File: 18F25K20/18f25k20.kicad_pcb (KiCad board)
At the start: 2 copper layers, 33 parts, among them P1 CONN_01X02, P2 ICSP, U1 18F25K20, U2 LM1117

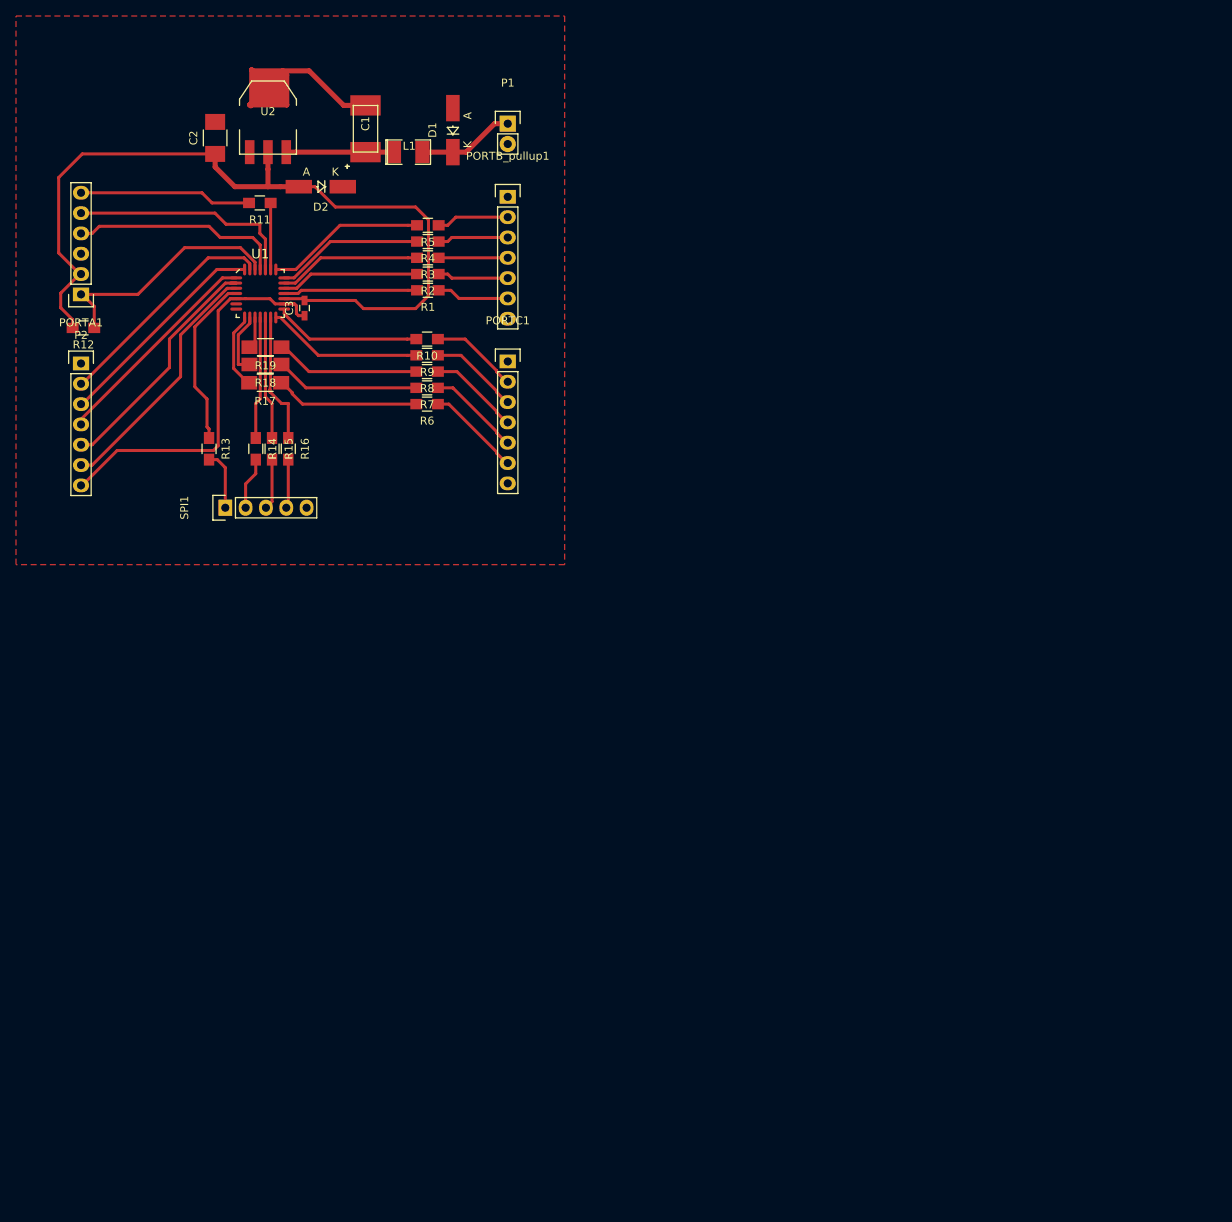
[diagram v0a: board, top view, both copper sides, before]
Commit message: PIC-ssop, sch &layout. TODO:modify pinheader+gnd polygon. 3.2mm holes
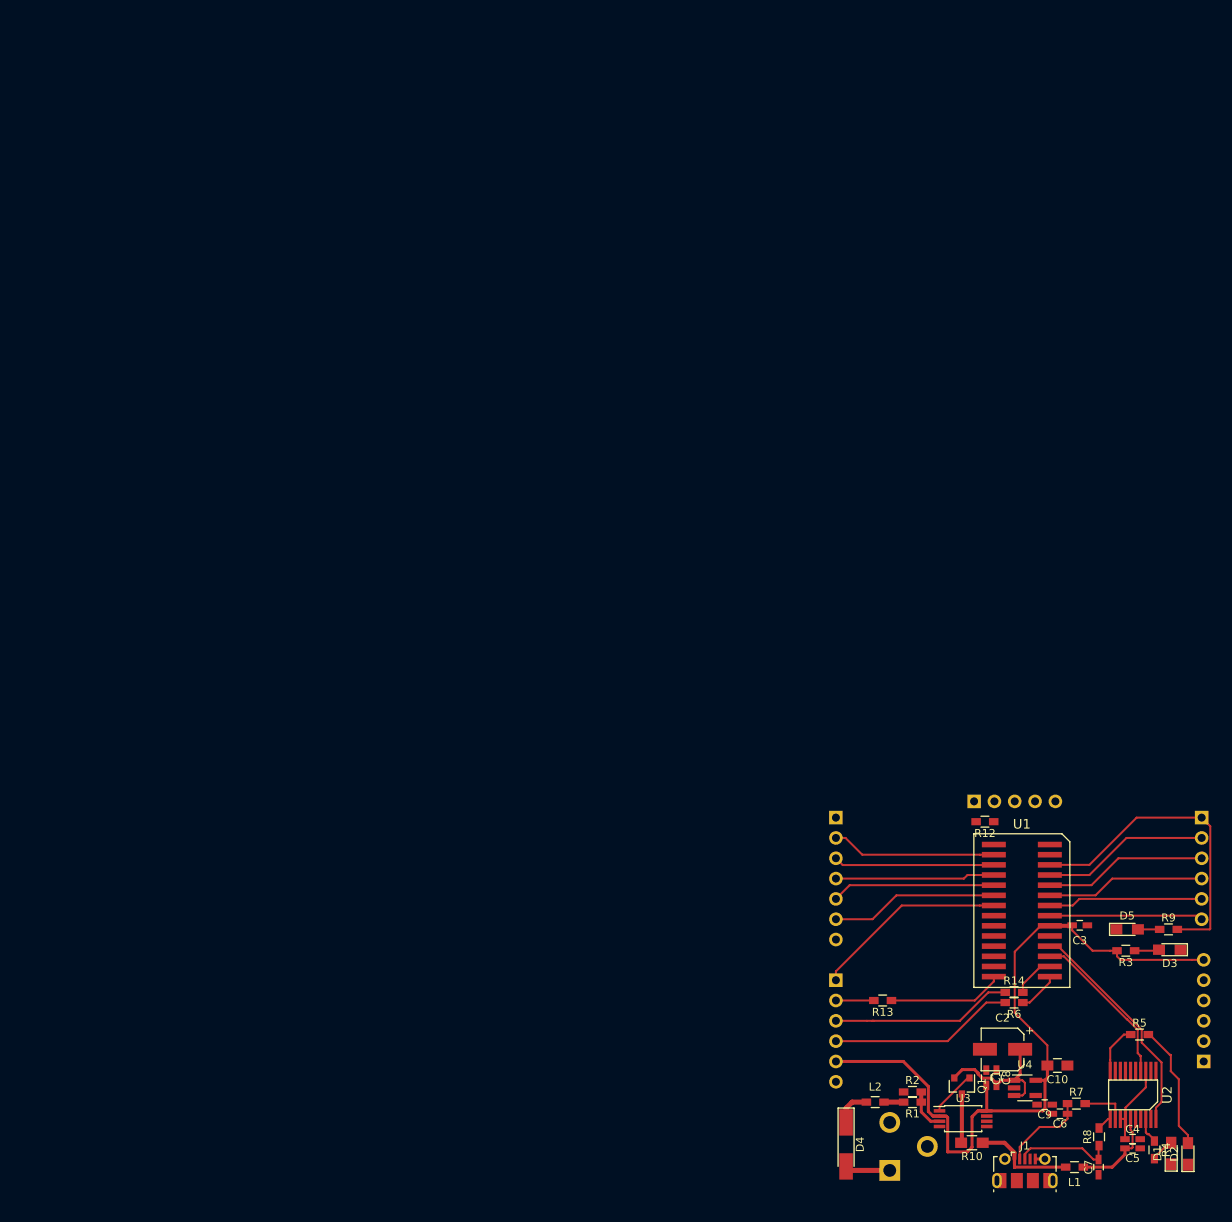
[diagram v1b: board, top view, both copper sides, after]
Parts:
- removed PORTA1, PORTB_pullup1, PORTC1: CONN_01X07, Pin_Headers:Pin_Header_Straight_1x07
- removed R11: 0, Resistors_SMD:R_0805_HandSoldering
- removed R15, R16: 220R, Resistors_SMD:R_0805_HandSoldering
- removed R17, R18, R19: 0, Resistors_SMD:R_1206_HandSoldering
- removed SPI1: CONN_01X05, Pin_Headers:Pin_Header_Straight_1x05
- added C10: 4u7, Capacitors_SMD:C_0805_HandSoldering, F.Cu at (219.5, 147.8)
- added C4: 100n, Capacitors_SMD:C_0603_HandSoldering, F.Cu at (228.9, 157.0)
- added C5: 100n, Capacitors_SMD:C_0603_HandSoldering, F.Cu at (228.9, 158.2)
- added C6: 47p, Capacitors_SMD:C_0603_HandSoldering, F.Cu at (219.8, 153.9)
- added C7: 47p, Capacitors_SMD:C_0603_HandSoldering, F.Cu at (224.6, 160.5)
- added C8: 1u, Capacitors_SMD:C_0603_HandSoldering, F.Cu at (211.8, 149.3)
- added C9: 10n, Capacitors_SMD:C_0603_HandSoldering, F.Cu at (217.9, 152.7)
- added D3: LED, LEDs:LED_0805_HandSoldering, F.Cu at (233.5, 133.3)
- added D4: LL4148, Diodes_SMD:D_MiniMELF_Handsoldering, F.Cu at (193.0, 157.7)
- added D5: LED, LEDs:LED_0805_HandSoldering, F.Cu at (228.2, 130.8)
- added J1: USB_OTG, Connectors_USB:USB_Micro-B_Molex-105017-0001, F.Cu at (215.4, 161.9)
- added J2: Barrel_Jack, Connectors:Barrel_Jack_CUI_PJ-102AH, B.Cu at (198.5, 160.9)
- added L2: FB, Inductors_SMD:L_0603_HandSoldering, F.Cu at (196.7, 152.4)
- added P3: PORTB, Pin_Headers:Pin_Header_Straight_1x06_Pitch2.54mm, B.Cu at (237.5, 116.8)
- added P4: PC_power, Pin_Headers:Pin_Header_Straight_1x06_Pitch2.54mm, B.Cu at (237.7, 147.3)
- added P5: ADC, Pin_Headers:Pin_Header_Straight_1x07_Pitch2.54mm, B.Cu at (191.8, 116.8)
- added Q1: FDN240P, TO_SOT_Packages_SMD:SOT-23, F.Cu at (207.5, 150.4)
- added U3: LM358, Housings_SSOP:TSSOP-8_4.4x3mm_Pitch0.65mm, F.Cu at (207.7, 154.5)
- added U4: LP2985-3.3, TO_SOT_Packages_SMD:SOT-23-5_HandSoldering, F.Cu at (215.4, 150.6)
- C1: value 100u -> 100n; footprint .pretty:2312_handsoldering -> Capacitors_SMD:C_0603_HandSoldering
- C2: value 33u -> 10u; footprint Capacitors_SMD:C_1210_HandSoldering -> Capacitors_SMD:CP_Elec_5x5.3
- D1: value 5V6 -> LED; footprint Diodes_SMD:MiniMELF_Handsoldering -> LEDs:LED_0805_HandSoldering
- D2: value LL914 -> LED; footprint Diodes_SMD:MiniMELF_Handsoldering -> LEDs:LED_0805_HandSoldering
- L1: value 4u7 -> FB; footprint SMD_Packages:SMD-1210_Pol -> Inductors_SMD:L_0603_HandSoldering
- P1: value CONN_01X02 -> SPI; footprint Pin_Headers:Pin_Header_Straight_1x02 -> Pin_Headers:Pin_Header_Straight_1x06_Pitch2.54mm; moved to B.Cu
- P2: footprint Pin_Headers:Pin_Header_Straight_1x06 -> Pin_Headers:Pin_Header_Straight_1x05_Pitch2.54mm; moved to B.Cu
- R1, R2: value 220R -> 10k; footprint Resistors_SMD:R_0805_HandSoldering -> Resistors_SMD:R_0603_HandSoldering
- R10: value 220R -> 0R
- R12, R13, R14, R6: footprint Resistors_SMD:R_0805_HandSoldering -> Resistors_SMD:R_0603_HandSoldering
- R3, R4, R5, R9: value 220R -> 270R; footprint Resistors_SMD:R_0805_HandSoldering -> Resistors_SMD:R_0603_HandSoldering
- R7, R8: value 220R -> 27R; footprint Resistors_SMD:R_0805_HandSoldering -> Resistors_SMD:R_0603_HandSoldering
- U1: value 18F25K20 -> 18F25K20_ssop; footprint .pretty:QFP_28 -> .pretty:SSOP-28_hand_solder
- U2: value LM1117 -> FTDI231x; footprint .pretty:SOT-223_handsoldering -> .pretty:SSOP-20_FTD23x
- moved D2 162.4 mm to (235.8, 158.9), turned to 90 degrees
- moved U2 156.8 mm to (225.2, 146.2), turned to 270 degrees
- moved D1 156.3 mm to (233.7, 158.8)
- moved L1 151.8 mm to (221.6, 160.5), turned to 180 degrees
- moved C2 150.5 mm to (212.6, 145.8), turned to 180 degrees
- moved R4 145.4 mm to (231.6, 158.4), turned to 270 degrees
- moved C1 141.9 mm to (210.6, 149.4), turned to 270 degrees
- moved R5 134.7 mm to (229.7, 144.0), turned to 0 degrees
- moved R12 128.5 mm to (210.4, 117.3)
- moved P2 128.4 mm to (209.0, 114.8), turned to 270 degrees
- moved R8 127.3 mm to (224.7, 156.7), turned to 90 degrees
- moved C3 123.9 mm to (222.2, 130.3), turned to 180 degrees
- moved R3 122.9 mm to (228.0, 133.5)
- moved U1 122.5 mm to (215.0, 128.5), turned to 270 degrees
- moved R10 121.4 mm to (208.8, 157.5)
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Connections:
- C1 pad 1: Net-(C1-Pad1) -> GND
- C1 pad 2: GND -> VCC
- C2 pad 1: Net-(C2-Pad1) -> /Vin
- C3 pad 2: Net-(C2-Pad1) -> VCC
- D1 pad 1: Net-(D1-Pad1) -> GND
- D1 pad 2: GND -> Net-(D1-Pad2)
- D2 pad 1: Net-(D2-Pad1) -> GND
- D2 pad 2: Net-(C2-Pad1) -> Net-(D2-Pad2)
- L1 pad 1: Net-(C1-Pad1) -> Net-(C5-Pad2)
- L1 pad 2: Net-(D1-Pad1) -> Net-(J1-Pad1)
- P1 pad 1: Net-(D1-Pad1) -> /SS
- P1 pad 2: GND -> /SCK
- P2 pad 2: Net-(C2-Pad1) -> VCC
- R1 pad 1: Net-(PORTB_pullup1-Pad6) -> /Vin_cmp
- R1 pad 2: Net-(R1-Pad2) -> /ps
- R10 pad 1: Net-(PORTC1-Pad2) -> /Vusb
- R10 pad 2: Net-(R10-Pad2) -> Net-(C5-Pad2)
- R12 pad 2: Net-(C2-Pad1) -> VCC
- R13 pad 1: Net-(R13-Pad1) -> /SCK
- R13 pad 2: Net-(R13-Pad2) -> /SCK
- R14 pad 1: Net-(R14-Pad1) -> /SDO
- R14 pad 2: Net-(R14-Pad2) -> /SDO
- R2 pad 1: Net-(PORTB_pullup1-Pad5) -> GND
- R2 pad 2: Net-(R2-Pad2) -> /Vin_cmp
- R3 pad 2: Net-(R3-Pad2) -> VCC
- R4 pad 1: Net-(PORTB_pullup1-Pad3) -> /Rx_led
- R4 pad 2: Net-(R4-Pad2) -> Net-(D1-Pad2)
- R5 pad 1: Net-(PORTB_pullup1-Pad2) -> /Tx_led
- R5 pad 2: Net-(R5-Pad2) -> Net-(D2-Pad2)
- R6 pad 1: Net-(PORTC1-Pad6) -> /SDI
- R6 pad 2: Net-(R17-Pad1) -> /SDI
- R7 pad 2: Net-(R18-Pad1) -> /D-
- R8 pad 2: Net-(R19-Pad1) -> /D+
- R9 pad 2: Net-(R9-Pad2) -> /picled
- U1 pad 1: Net-(PORTA1-Pad4) -> Net-(P2-Pad1)
- U1 pad 10: Net-(R19-Pad2) -> (no net)
- U1 pad 11: Net-(R14-Pad1) -> Net-(P4-Pad3)
- U1 pad 14: Net-(R9-Pad2) -> /SCK
- U1 pad 15: Net-(R10-Pad2) -> /SDI
- U1 pad 16: GND -> /SDO
- U1 pad 17: Net-(C2-Pad1) -> /RXD
- U1 pad 18: Net-(R1-Pad2) -> /TXD
- U1 pad 19: Net-(R2-Pad2) -> GND
- U1 pad 20: Net-(R3-Pad2) -> VCC
- U1 pad 21: Net-(R4-Pad2) -> Net-(P3-Pad6)
- U1 pad 22: Net-(R5-Pad2) -> Net-(P3-Pad5)
- U1 pad 24: Net-(P2-Pad5) -> Net-(P3-Pad3)
- U1 pad 25: Net-(P2-Pad4) -> Net-(P3-Pad2)
- U1 pad 26: Net-(P2-Pad1) -> /picled
- U1 pad 27: Net-(PORTA1-Pad2) -> Net-(P2-Pad5)
- U1 pad 28: Net-(PORTA1-Pad3) -> Net-(P2-Pad4)
- U1 pad 4: Net-(R13-Pad1) -> Net-(P5-Pad4)
- U1 pad 5: GND -> Net-(P5-Pad5)
- U1 pad 7: Net-(U1-Pad7) -> /SS
- U1 pad 8: Net-(R17-Pad2) -> GND
- U1 pad 9: Net-(R18-Pad2) -> (no net)
- U2 pad 1: GND -> (no net)
- U2 pad 2: Net-(C2-Pad1) -> (no net)
- U2 pad 3: Net-(C1-Pad1) -> Net-(C4-Pad1)
- U2 pad 4: (no net) -> /RXD
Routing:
- net Net-(C2-Pad1): track 106.6 -> 0.00 mm
- net VCC: track 0.00 -> 93.6 mm
- net GND: track 88.3 -> 1.20 mm
- net /picled: track 0.00 -> 39.9 mm
- net Net-(P2-Pad1): track 30.8 -> 0.00 mm
- net /TXD: track 0.00 -> 29.4 mm
- net Net-(P2-Pad5): track 28.9 -> 0.00 mm
- net Net-(PORTA1-Pad2): track 28.7 -> 0.00 mm
- net /SDI: track 0.00 -> 28.3 mm
- net /SDO: track 0.00 -> 28.1 mm
- net Net-(PORTA1-Pad4): track 27.5 -> 0.00 mm
- net Net-(PORTA1-Pad3): track 27.4 -> 0.00 mm
- net Net-(P2-Pad4): track 26.8 -> 0.00 mm
- net /SS: track 0.00 -> 24.3 mm
- net Net-(P2-Pad6): track 21.5 -> 0.00 mm
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- removed copper zone on F.Cu, net GND
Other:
- net class Default: clearance 0.2 -> 0.1
- net class tr: clearance 0.2 -> 0.1
- rule trace_clearance: 0.2 -> 0.1

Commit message: layout&vias
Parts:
- removed R10: 0R, Resistors_SMD:R_0805_HandSoldering
- added C11: 4u7, Capacitors_SMD:C_0805_HandSoldering, F.Cu at (234.2, 138.9)
- added L3: FB, Inductors_SMD:L_0603_HandSoldering, F.Cu at (208.8, 157.6)
- added R11: 0R, Resistors_SMD:R_0805_HandSoldering, F.Cu at (195.1, 132.4)
- added REF**: R_1206, Resistors_SMD:R_1206, F.Cu at (229.7, 142.0)
- added REF**: M3_hole, buradar:M3_hole, F.Cu at (236.0, 160.3)
- added REF** (x2): M3_hole, buradar:M3_hole, F.Cu at (200.7, 146.1)
- added REF**: M3_hole, buradar:M3_hole, F.Cu at (193.3, 112.8)
- added REF**: M3_hole, buradar:M3_hole, F.Cu at (236.0, 112.8)
- P1: footprint Pin_Headers:Pin_Header_Straight_1x06_Pitch2.54mm -> Pin_Headers:Pin_Header_Straight_1x09_Pitch2.54mm
- P4: value PC_power -> power supply; footprint Pin_Headers:Pin_Header_Straight_1x06_Pitch2.54mm -> Pin_Headers:Pin_Header_Straight_1x04_Pitch2.54mm
- moved D4 5.98 mm to (198.9, 158.8), turned to 180 degrees
- moved D2 5.46 mm to (236.7, 153.5)
- moved J2 5.42 mm to (197.1, 155.7), turned to 180 degrees
- moved D1 5.36 mm to (234.2, 153.5)
- moved P4 2.55 mm to (237.5, 144.8)
- moved P2 2.27 mm to (210.1, 112.8)
- moved P1 1.78 mm to (191.8, 135.4)
- moved R12 1.08 mm to (211.2, 116.6), turned to 0 degrees
- moved R13 0.64 mm to (198.2, 140.0)
- turned R14 to 180 degrees
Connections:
- P1 pad 2: /SCK -> /RC0
- P1 pad 3: /SDO -> /RC1
- P1 pad 4: /SDI -> /RC2
- P1 pad 5: VCC -> /SCK
- P1 pad 6: GND -> /SDO
- P4 pad 1: Net-(P4-Pad1) -> GND
- P4 pad 2: Net-(P4-Pad2) -> GND
- P4 pad 3: Net-(P4-Pad3) -> GND
- P4 pad 4: GND -> VCC
- R13 pad 1: /SCK -> Net-(R13-Pad1)
- R14 pad 1: /SDO -> Net-(R14-Pad1)
- R6 pad 1: /SDI -> Net-(R6-Pad1)
- U1 pad 11: Net-(P4-Pad3) -> /RC0
- U1 pad 12: Net-(P4-Pad2) -> /RC1
- U1 pad 13: Net-(P4-Pad1) -> /RC2
- U1 pad 14: /SCK -> Net-(R13-Pad1)
- U1 pad 15: /SDI -> Net-(R6-Pad1)
- U1 pad 16: /SDO -> Net-(R14-Pad1)
- U1 pad 7: /SS -> Net-(R11-Pad1)
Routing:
- net GND: track 1.20 -> 163.7 mm
- net /RC2: track 0.00 -> 22.9 mm
- net /RC1: track 0.00 -> 22.6 mm
- net /RC0: track 0.00 -> 21.8 mm
- net /SS: track 24.3 -> 4.20 mm
- net Net-(R11-Pad1): track 0.00 -> 17.8 mm
- net Net-(R13-Pad1): track 0.00 -> 13.6 mm
- net Net-(P2-Pad5): track 0.00 -> 13.0 mm
- net /SCK: track 19.1 -> 7.89 mm
- net Net-(P2-Pad1): track 0.00 -> 8.95 mm
- net Net-(P2-Pad4): track 0.00 -> 8.92 mm
- net Net-(D4-Pad1): track 4.63 -> 12.0 mm
- net Net-(D1-Pad2): track 3.01 -> 9.59 mm
- net Net-(C5-Pad2): track 17.4 -> 11.3 mm
- net VCC: track 93.6 -> 99.5 mm
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- added copper zone on F.Cu, net GND
